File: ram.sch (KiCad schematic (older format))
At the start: 40 parts, among them U38 4164, U39 4164, U40 4164, U41 4164, U42 4164, U43 4164, U44 4164, U45 4164, U46 4164, U47 4164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

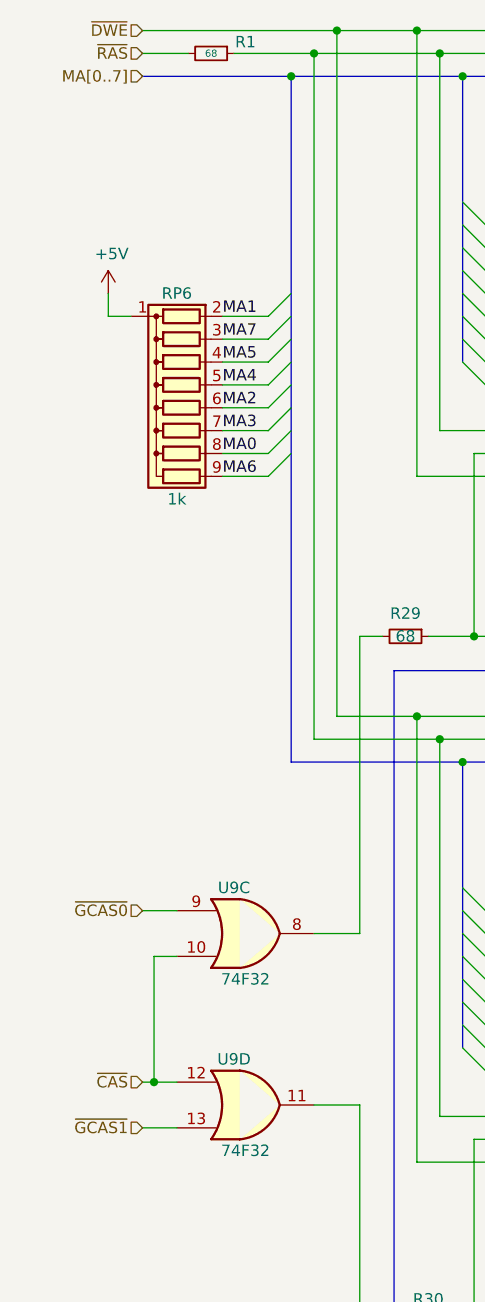
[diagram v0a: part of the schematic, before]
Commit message: Clean up schematic
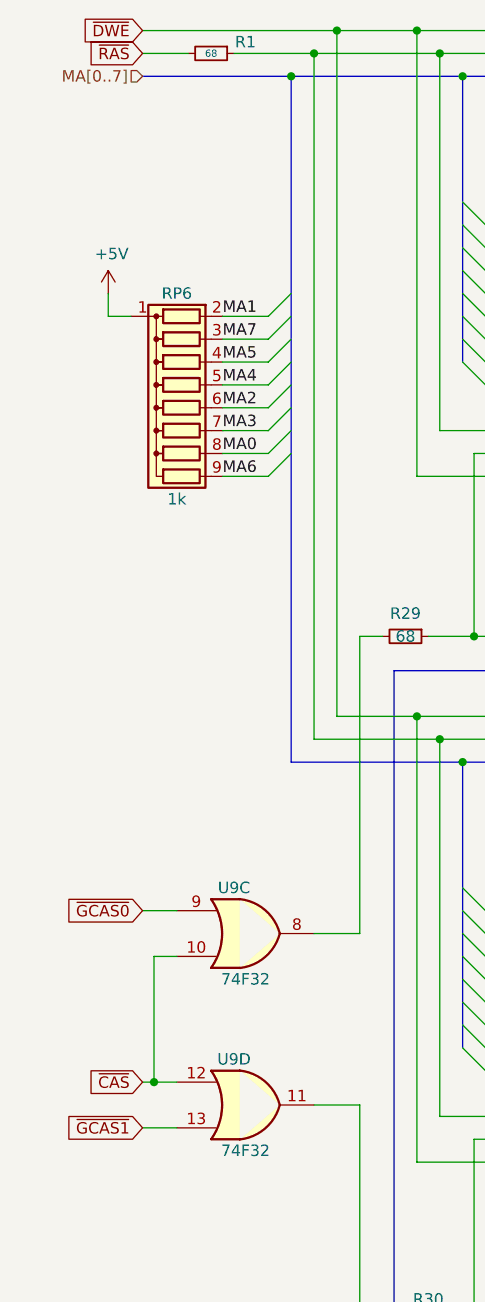
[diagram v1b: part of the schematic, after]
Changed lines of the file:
@@
 	1    0    0    -1
 $EndComp
-Text HLabel 1000 650  0    50   Input ~ 0
-~RAS
 Wire Wire Line
 	1000 650  1200 650
@@
 	10000 650  8900 650
 Connection ~ 8900 650
-Text HLabel 1000 550  0    50   Input ~ 0
-~DWE
 Wire Wire Line
 	1000 550  1850 550
@@
 	1    0    0    -1
 $EndComp
-Text HLabel 1000 5150 0    50   Input ~ 0
-~CAS
 Wire Wire Line
 	1000 5150 1050 5150
@@
 Wire Wire Line
 	1050 5150 1150 5150
-Text HLabel 1000 4400 0    50   Input ~ 0
-~GCAS0
 Wire Wire Line
 	1000 4400 1150 4400
-Text HLabel 1000 5350 0    50   Input ~ 0
-~GCAS1
 Wire Wire Line
 	1000 5350 1150 5350
@@
 Wire Bus Line
 	2100 3350 10550 3350
+Text GLabel 1000 5150 0    50   Input ~ 0
+~CAS
+Text GLabel 1000 550  0    50   Input ~ 0
+~DWE
+Text GLabel 1000 650  0    50   Input ~ 0
+~RAS
+Text GLabel 1000 4400 0    50   Input ~ 0
+~GCAS0
+Text GLabel 1000 5350 0    50   Input ~ 0
+~GCAS1
 $EndSCHEMATC
